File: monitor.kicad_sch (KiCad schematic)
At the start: 54 parts, among them U701 OPA2189D, U702 OPA2388D, U703 OPA2189D, U704 OPA2197xD, U705 OPA2197xD, U71 TMUX6208PWR, U72 TMUX6208PWR

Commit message: Little simplifications etc.
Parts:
- C? (x2): value 10n -> 1n
- R? (x2): value 100 -> 10
- R? (x2): value 22k -> 33k
- R?: value 13k -> 16k
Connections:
- net BufA: no longer names the net of J?.1 (Pin_1), R?.2, R?.2, RN71.5 (R4.2)
- net BufB: no longer names the net of J?.1 (Pin_1), R?.2, R?.2, RN71.7 (R2.2)
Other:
- moved on the sheet: C?, U702B, U702C

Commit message: Schematic complete, maybe
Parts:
- added C706, C707, C708, C709, C714, C715: 0u1, Capacitor_SMD:C_0402_1005Metric, symbol Device:C
- C701, C702, C703, C704: renamed from C?; footprint (none) -> Capacitor_SMD:C_0603_1608Metric; now left out of the parts list
- C705: renamed from C?; footprint (none) -> Capacitor_SMD:C_0603_1608Metric; LCSC (none) -> C307500
- C710, C711, C712, C713, C716, C717, C718, C719: renamed from C?; value 100n -> 0u1; footprint (none) -> Capacitor_SMD:C_0402_1005Metric; LCSC (none) -> C307331
- R701: renamed from R?; value 100 -> 10
- R702: renamed from R?; value 10 -> 100
- RN71: LCSC (none) -> C1358072; now left out of the parts list
- U701, U703: LCSC (none) -> C881489; now left out of the parts list
- U702: LCSC (none) -> C1517414
- U704: renamed from U705; LCSC (none) -> C139363; now left out of the parts list
- U704: LCSC (none) -> C139363; now left out of the parts list
- U71, U72: value TMUX6208PWR -> TMUX6104; footprint PW0016A-IPC_A -> Package_SO:TSSOP-14_4.4x5mm_P0.65mm; symbol Parts:TMUX6208PWR -> Parts:TMUX6104; LCSC (none) -> C2673388
- gave numbers to parts that had none: 31
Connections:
- net +18V: now also U71.12 (VDD), U72.12 (VDD), C706.1, C708.1, C714.1; no longer U71.13 (VDD), U72.13 (VDD)
- net +2V5: no longer U71.1 (A0), U72.1 (A0)
- net -18V: now also C707.2, C709.2, C715.2
- net GND: no longer U71.10 (S7), U71.12 (S5), U71.4 (S1), U71.6 (S3), U72.10 (S7), U72.12 (S5), U72.4 (S1), U72.6 (S3)
- net GNDPWR: now also U704.5 (+), U71.13 (GND), U72.13 (GND), C706.2, C707.1, C708.2, C709.1, C714.2, C715.1; no longer U704.3 (+), U71.14 (GND), U72.14 (GND)
- net IN_A1: now also U71.4 (S1); no longer U71.5 (S2)
- net IN_A2: now also U71.5 (S2); no longer U71.7 (S4)
- net IN_B1: now also U72.4 (S1); no longer U72.5 (S2)
- net IN_B2: now also U72.5 (S2); no longer U72.7 (S4)
- net SelA1: now also U71.14 (A1); no longer U71.16 (A1)
- net SelB1: now also U72.14 (A1); no longer U72.16 (A1)
- net TC+: now also U704.7; no longer U704.1
- net at C703.1, JP704.1 (A), RN71.6 (R3.2)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: now also C705.2; no longer C705.1
- net at JP702.1 (A): now also U72.6 (D); no longer U72.8 (D)
- net at R711.1, R712.2: now also U704.6 (-); no longer U704.2 (-)
- net at JP701.1 (A): now also U71.6 (D); no longer U71.8 (D)
- net at R708.1: now also C705.1; no longer C705.2
- removed net SelA2: U71.15 (A2)
- removed net SelB2: U72.15 (A2)
- new net SelA0: U71.1 (A0)
- new net SelB0: U72.1 (A0)
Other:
- moved on the sheet: C705, C710, C711, C712, C713, C716, C717, JP701, JP702, R710, R712, U701C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

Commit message: Part selection
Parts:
- J71, J72, J73, J74, J75: now left out of the parts list
- R701, R704: footprint (none) -> Resistor_SMD:R_0402_1005Metric; LCSC (none) -> C25077
- R702, R703: footprint (none) -> Resistor_SMD:R_0402_1005Metric; LCSC (none) -> C25076
- R705: footprint (none) -> Resistor_SMD:R_0603_1608Metric; LCSC (none) -> C23140
- R706, R711, R712: footprint (none) -> Resistor_SMD:R_0603_1608Metric; LCSC (none) -> C4216
- R707, R708: footprint (none) -> Resistor_SMD:R_0603_1608Metric; LCSC (none) -> C22978
- R709: footprint (none) -> Resistor_SMD:R_0603_1608Metric; LCSC (none) -> C22818
- R710: footprint (none) -> Resistor_SMD:R_0402_1005Metric; LCSC (none) -> C25741
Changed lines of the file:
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@@
 			)
 		)
-		(property "Footprint" ""
+		(property "Footprint" "Resistor_SMD:R_0402_1005Metric"
 			(at 124.46 90.932 90)
 			(effects
@@
 			)
 		)
-		(property "Datasheet" ""
+		(property "Datasheet" "~"
 			(at 124.46 92.71 0)
 			(effects
@@
 			)
 		)
+		(property "LCSC" "C25077"
+			(at 124.46 92.71 90)
+			(effects
+				(font
+					(size 1.27 1.27)
+				)
+				(hide yes)
+			)
+		)
 		(pin "2"
 		)
@@
 		(unit 1)
 		(exclude_from_sim no)
-		(in_bom yes)
+		(in_bom no)
 		(on_board yes)
 		(dnp no)
@@
 		(unit 1)
 		(exclude_from_sim no)
-		(in_bom yes)
+		(in_bom no)
 		(on_board yes)
 		(dnp no)
@@
 		(unit 1)
 		(exclude_from_sim no)
-		(in_bom yes)
+		(in_bom no)
 		(on_board yes)
 		(dnp no)
@@
 			)
 		)
-		(property "Footprint" ""
+		(property "Footprint" "Resistor_SMD:R_0603_1608Metric"
 			(at 171.45 89.408 90)
 			(effects
@@
 			)
 		)
+		(property "LCSC" "C22978"
+			(at 171.45 87.63 90)
+			(effects
+				(font
+					(size 1.27 1.27)
+				)
+				(hide yes)
+			)
+		)
 		(pin "2"
 		)
@@
 			)
 		)
-		(property "Footprint" ""
+		(property "Footprint" "Resistor_SMD:R_0603_1608Metric"
 			(at 198.12 116.078 90)
 			(effects
@@
 			)
 		)
+		(property "LCSC" "C4216"
+			(at 198.12 114.3 90)
+			(effects
+				(font
+					(size 1.27 1.27)
+				)
+				(hide yes)
+			)
+		)
 		(pin "2"
 		)
@@
 		(unit 1)
 		(exclude_from_sim no)
-		(in_bom yes)
+		(in_bom no)
 		(on_board yes)
 		(dnp no)
@@
 			)
 		)
-		(property "Footprint" ""
+		(property "Footprint" "Resistor_SMD:R_0402_1005Metric"
 			(at 124.46 81.788 90)
 			(effects
@@
 			)
 		)
-		(property "Datasheet" ""
+		(property "Datasheet" "~"
 			(at 124.46 80.01 0)
 			(effects
@@
 			)
 		)
+		(property "LCSC" "C25076"
+			(at 124.46 80.01 90)
+			(effects
+				(font
+					(size 1.27 1.27)
+				)
+				(hide yes)
+			)
+		)
 		(pin "2"
 		)
@@
 			)
 		)
-		(property "Footprint" ""
+		(property "Footprint" "Resistor_SMD:R_0603_1608Metric"
 			(at 158.75 98.552 90)
 			(effects
@@
 			)
 		)
+		(property "LCSC" "C4216"
+			(at 158.75 100.33 90)
+			(effects
+				(font
+					(size 1.27 1.27)
+				)
+				(hide yes)
+			)
+		)
 		(pin "2"
 		)
@@
 			)
 		)
-		(property "Footprint" ""
+		(property "Footprint" "Resistor_SMD:R_0402_1005Metric"
 			(at 124.46 83.312 90)
 			(effects
@@
 			)
 		)
-		(property "Datasheet" ""
+		(property "Datasheet" "~"
 			(at 124.46 85.09 0)
 			(effects
@@
 			)
 		)
+		(property "LCSC" "C25076"
+			(at 124.46 85.09 90)
+			(effects
+				(font
+					(size 1.27 1.27)
+				)
+				(hide yes)
+			)
+		)
 		(pin "2"
 		)
@@
 			)
 		)
-		(property "Footprint" ""
+		(property "Footprint" "Resistor_SMD:R_0402_1005Metric"
 			(at 124.46 74.168 90)
 			(effects
@@
 			)
 		)
-		(property "Datasheet" ""
+		(property "Datasheet" "~"
 			(at 124.46 72.39 0)
 			(effects
@@
 			)
 		)
+		(property "LCSC" "C25077"
+			(at 124.46 72.39 90)
+			(effects
+				(font
+					(size 1.27 1.27)
+				)
+				(hide yes)
+			)
+		)
 		(pin "2"
 		)
@@
 			)
 		)
-		(property "Footprint" ""
+		(property "Footprint" "Resistor_SMD:R_0402_1005Metric"
 			(at 185.42 123.698 90)
 			(effects
@@
 			)
 		)
-		(property "Datasheet" "Easy swap"
+		(property "Datasheet" "~"
 			(at 185.42 121.92 0)
 			(effects
@@
 			)
 		)
+		(property "LCSC" "C25741"
+			(at 185.42 121.92 90)
+			(effects
+				(font
+					(size 1.27 1.27)
+				)
+				(hide yes)
+			)
+		)
 		(pin "2"
 		)
@@
 			)
 		)
-		(property "Footprint" ""
+		(property "Footprint" "Resistor_SMD:R_0603_1608Metric"
 			(at 152.908 106.68 90)
 			(effects
@@
 			)
 		)
+		(property "LCSC" "C23140"
+			(at 151.13 106.68 90)
+			(effects
+				(font
+					(size 1.27 1.27)
+				)
+				(hide yes)
+			)
+		)
 		(pin "2"
 		)
@@
 			)
 		)
-		(property "Footprint" ""
+		(property "Footprint" "Resistor_SMD:R_0603_1608Metric"
 			(at 172.72 118.618 90)
 			(effects
@@
 			)
 		)
-		(property "Datasheet" "Easy swap"
+		(property "Datasheet" "~"
 			(at 172.72 116.84 0)
 			(effects
@@
 			)
 		)
+		(property "LCSC" "C22818"
+			(at 172.72 116.84 90)
+			(effects
+				(font
+					(size 1.27 1.27)
+				)
+				(hide yes)
+			)
+		)
 		(pin "2"
 		)
@@
 			)
 		)
-		(property "Footprint" ""
+		(property "Footprint" "Resistor_SMD:R_0603_1608Metric"
 			(at 215.9 123.698 90)
 			(effects
@@
 			)
 		)
+		(property "LCSC" "C4216"
+			(at 215.9 121.92 90)
+			(effects
+				(font
+					(size 1.27 1.27)
+				)
+				(hide yes)
+			)
+		)
 		(pin "2"
 		)
@@
 			)
 		)
-		(property "Footprint" ""
+		(property "Footprint" "Resistor_SMD:R_0603_1608Metric"
 			(at 181.61 93.472 90)
 			(effects
@@
 			)
 		)
+		(property "LCSC" "C22978"
+			(at 181.61 95.25 90)
+			(effects
+				(font
+					(size 1.27 1.27)
+				)
+				(hide yes)
+			)
+		)
 		(pin "2"
 		)
@@
 		(unit 1)
 		(exclude_from_sim no)
-		(in_bom yes)
+		(in_bom no)
 		(on_board yes)
 		(dnp no)

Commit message: ERC passes.
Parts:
- C703, C704: value 100p -> 0n1
- RN71: value 10k × 4 -> LT5400-1; footprint (none) -> Package_SO:MSOP-8-1EP_3x3mm_P0.65mm_EP1.68x1.88mm; symbol Device:R_Pack04 -> Parts:LT5400; R1 (none) -> 10k; R2 (none) -> 10k; R3 (none) -> 10k; R4 (none) -> 10k; now in the parts list
- U704: value OPA2197xD -> OPA2197D
- U76: renamed from U701; value OPA2189D -> OPA2189DGK; footprint Package_SO:SOIC-8_3.9x4.9mm_P1.27mm -> Package_SO:MSOP-8_3x3mm_P0.65mm; symbol Parts:OPA2189D -> Parts:OPA2189DGK
- U77: renamed from U702; value OPA2388D -> OPA2388DGK; footprint Package_SO:SOIC-8_3.9x4.9mm_P1.27mm -> Package_SO:MSOP-8_3x3mm_P0.65mm; symbol Parts:OPA2388D -> Parts:OPA2388DGK; now left out of the parts list
- U78: renamed from U703; value OPA2189D -> OPA2189DGK; footprint Package_SO:SOIC-8_3.9x4.9mm_P1.27mm -> Package_SO:MSOP-8_3x3mm_P0.65mm; symbol Parts:OPA2189D -> Parts:OPA2189DGK
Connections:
- net GNDPWR: now also RN71.9
- net TC+: now also RN71.5; no longer RN71.1 (R1.1)
- net TC-: now also RN71.4; no longer RN71.8 (R1.2)
- net at J74.1 (Pin_1), R703.2, R704.2: now also RN71.3; no longer RN71.7 (R2.2)
- net at C703.1, C705.2, JP704.1 (A)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: now also RN71.2; no longer RN71.6 (R3.2)
- net at J73.1 (Pin_1), R701.2, R702.2: now also RN71.1; no longer RN71.5 (R4.2)
- new net: C703.2, RN71.6, RN71.7, RN71.8, U77.3 (+)
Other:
- moved on the sheet: C703, R705

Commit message: Everything assigned except for wierd shit.
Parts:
- removed C716, C717: 0u1, Capacitor_SMD:C_0402_1005Metric, symbol Device:C
- removed JP701, JP702: SolderJumper_2_Bridged, symbol Jumper:SolderJumper_2_Bridged
- removed JP705, JP706, JP707, JP708, JP709, JP710, JP711, JP712, JP713, JP714, JP715, JP716: SolderJumper_2_Open, symbol Jumper:SolderJumper_2_Open
- C703: value 0n1 -> 3n3; now fitted
- C704: value 0n1 -> 330p; LCSC (none) -> C1664; now fitted; now in the parts list
- C705: value 10n -> 1n; LCSC C307500 -> (none); now left out of the parts list
- JP703: footprint (none) -> Parts:ThermJump
- R705: value 33 -> 100
- R706: value 33k -> 10k; LCSC C4216 -> (none)
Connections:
- net AddendA: now also U71.6 (D)
- net AddendB: now also U72.6 (D)
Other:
- moved on the sheet: J71, J72, J73, J75, JP703, JP704

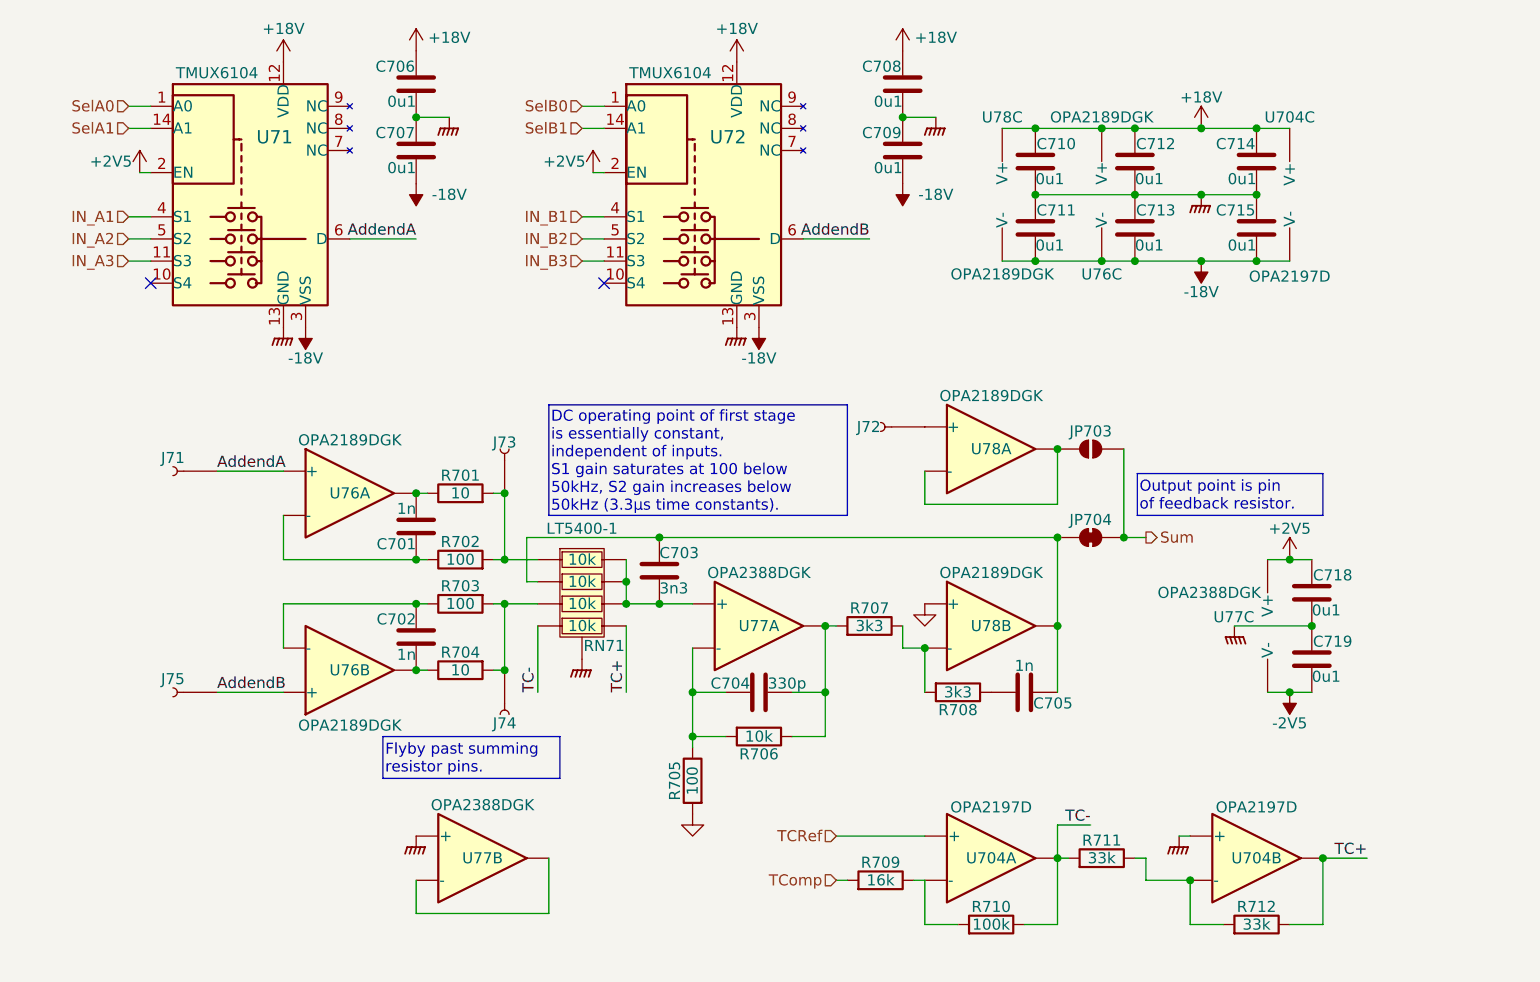
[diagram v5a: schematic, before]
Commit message: Layout underway
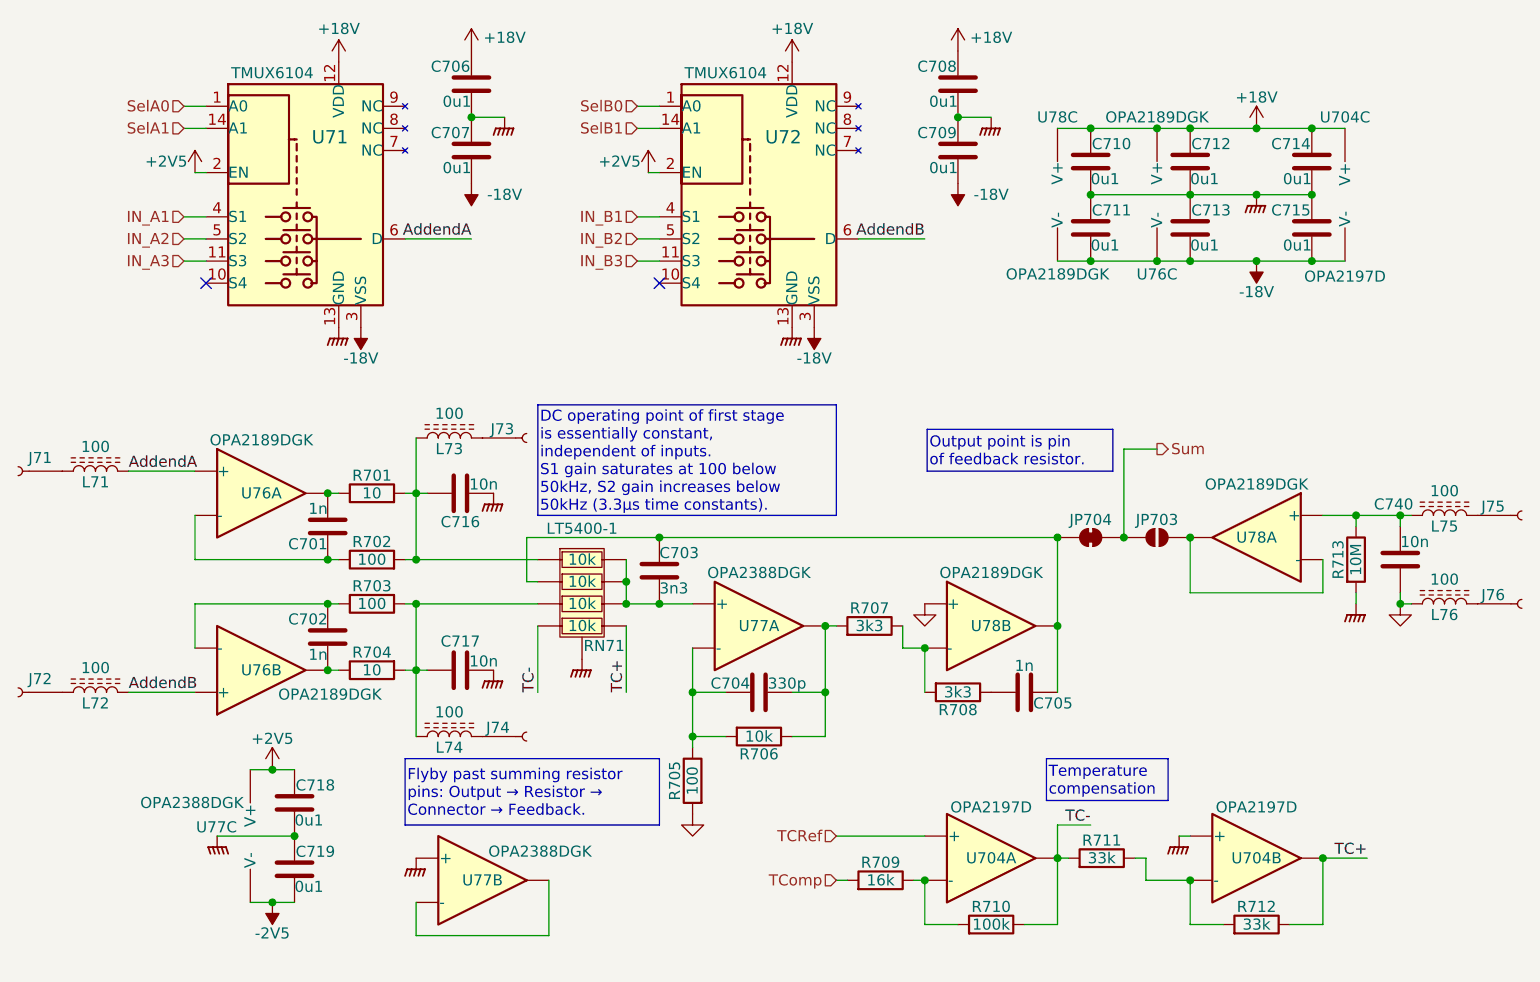
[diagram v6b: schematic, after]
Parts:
- added C716, C717, C740: 10n, Capacitor_SMD:C_0603_1608Metric, symbol Device:C
- added J76: Conn_01x01_Socket, TestPoint:TestPoint_Plated_Hole_D5.0mm, symbol Connector:Conn_01x01_Socket
- added L71, L72, L73, L74, L75, L76: 100, Inductor_SMD:L_0603_1608Metric, symbol Device:L_Ferrite
- added R713: 10M, Resistor_SMD:R_0603_1608Metric, symbol Device:R
- J71, J73, J74: footprint (none) -> TestPoint:TestPoint_Plated_Hole_D5.0mm
- J72: renamed from J75; footprint (none) -> TestPoint:TestPoint_Plated_Hole_D5.0mm
- J75: renamed from J72; footprint (none) -> TestPoint:TestPoint_Plated_Hole_D5.0mm
- JP703: footprint Parts:ThermJump -> Parts:ThermJump_1
- JP704: footprint (none) -> Parts:ThermJumpBridge
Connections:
- net AddendA: now also L71.2; no longer J71.1 (Pin_1)
- net AddendB: now also L72.2; no longer J72.1 (Pin_1)
- net GND: now also C740.2, L76.1
- net GNDPWR: now also C716.1, C717.1, R713.2
- net at U78.3 (+): now also C740.1, L75.1, R713.1; no longer J75.1 (Pin_1)
- net at R703.2, R704.2, RN71.3: now also C717.2, L74.1; no longer J74.1 (Pin_1)
- net at R701.2, R702.2, RN71.1: now also C716.2, L73.1; no longer J73.1 (Pin_1)
- new net: J74.1 (Pin_1), L74.2
- new net: J73.1 (Pin_1), L73.2
- new net: J76.1 (Pin_1), L76.2
- new net: J71.1 (Pin_1), L71.1
- new net: J72.1 (Pin_1), L72.1
- new net: J75.1 (Pin_1), L75.2
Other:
- moved on the sheet: C701, C702, C706, C707, C708, C709, C710, C711, C712, C713, C714, C715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

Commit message: Whew.  DACs routed
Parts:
- R706: LCSC (none) -> C25804
- U704: footprint Package_SO:SOIC-8_3.9x4.9mm_P1.27mm -> Parts:OPA2197; symbol Amplifier_Operational:OPA2197xD -> Parts:OPA2197D
- U76, U78: footprint Package_SO:MSOP-8_3x3mm_P0.65mm -> Parts:OPA2189
- U77: footprint Package_SO:MSOP-8_3x3mm_P0.65mm -> Parts:OPA2388
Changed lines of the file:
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@@
 			)
 		)
-		(property "Footprint" "Package_SO:MSOP-8_3x3mm_P0.65mm"
+		(property "Footprint" "Parts:OPA2189"
 			(at 217.17 77.47 0)
 			(effects
@@
 			)
 		)
-		(property "Footprint" "Package_SO:MSOP-8_3x3mm_P0.65mm"
+		(property "Footprint" "Parts:OPA2189"
 			(at 100.33 92.71 0)
 			(effects
@@
 			)
 		)
-		(property "Footprint" "Package_SO:MSOP-8_3x3mm_P0.65mm"
+		(property "Footprint" "Parts:OPA2189"
 			(at 191.77 38.1 0)
 			(effects
@@
 	)
 	(symbol
-		(lib_name "OPA2197xD_1")
-		(lib_id "Amplifier_Operational:OPA2197xD")
+		(lib_id "Parts:OPA2197D")
 		(at 215.9 114.3 0)
 		(unit 2)
@@
 			)
 		)
-		(property "Footprint" "Package_SO:SOIC-8_3.9x4.9mm_P1.27mm"
+		(property "Footprint" "Parts:OPA2197"
 			(at 218.44 114.3 0)
 			(effects
@@
 			)
 		)
-		(property "Datasheet" "1A working"
+		(property "Datasheet" "2A / 50mOhm"
 			(at 82.55 69.85 0)
 			(effects
@@
 	)
 	(symbol
-		(lib_id "Amplifier_Operational:OPA2197xD")
+		(lib_id "Parts:OPA2197D")
 		(at 226.06 38.1 0)
 		(unit 3)
@@
 			)
 		)
-		(property "Footprint" "Package_SO:SOIC-8_3.9x4.9mm_P1.27mm"
+		(property "Footprint" "Parts:OPA2197"
 			(at 228.6 38.1 0)
 			(effects
@@
 			)
 		)
-		(property "LCSC" ""
+		(property "LCSC" "C25804"
 			(at 158.75 100.33 90)
 			(effects
@@
 			)
 		)
-		(property "Datasheet" "1A working"
+		(property "Datasheet" "2A / 50mOhm"
 			(at 237.49 85.09 0)
 			(effects
@@
 			)
 		)
-		(property "Datasheet" "~"
+		(property "Datasheet" "C0G"
 			(at 147.32 81.28 0)
 			(effects
@@
 			)
 		)
-		(property "Datasheet" "1A working"
+		(property "Datasheet" "2A / 50mOhm"
 			(at 123.19 100.33 0)
 			(effects
@@
 			)
 		)
-		(property "Footprint" "Package_SO:MSOP-8_3x3mm_P0.65mm"
+		(property "Footprint" "Parts:OPA2189"
 			(at 203.2 38.1 0)
 			(effects
@@
 			)
 		)
-		(property "Datasheet" "1A working"
+		(property "Datasheet" "2A / 50mOhm"
 			(at 123.19 66.04 0)
 			(effects
@@
 	)
 	(symbol
-		(lib_name "OPA2388DGK_2")
 		(lib_id "Parts:OPA2388DGK")
 		(at 158.75 87.63 0)
@@
 			)
 		)
-		(property "Footprint" "Package_SO:MSOP-8_3x3mm_P0.65mm"
+		(property "Footprint" "Parts:OPA2388"
 			(at 161.29 87.63 0)
 			(effects
@@
 			)
 		)
-		(property "Footprint" "Package_SO:MSOP-8_3x3mm_P0.65mm"
+		(property "Footprint" "Parts:OPA2388"
 			(at 97.79 111.76 0)
 			(effects
@@
 	)
 	(symbol
-		(lib_name "OPA2197xD_2")
-		(lib_id "Amplifier_Operational:OPA2197xD")
+		(lib_id "Parts:OPA2197D")
 		(at 185.42 114.3 0)
 		(unit 1)
@@
 			)
 		)
-		(property "Footprint" "Package_SO:SOIC-8_3.9x4.9mm_P1.27mm"
+		(property "Footprint" "Parts:OPA2197"
 			(at 187.96 114.3 0)
 			(effects
@@
 			)
 		)
-		(property "Datasheet" "1A working"
+		(property "Datasheet" "2A / 50mOhm"
 			(at 237.49 74.93 0)
 			(effects
@@
 			)
 		)
-		(property "Datasheet" "1A working"
+		(property "Datasheet" "2A / 50mOhm"
 			(at 82.55 95.25 0)
 			(effects
@@
 			)
 		)
-		(property "Footprint" "Package_SO:MSOP-8_3x3mm_P0.65mm"
+		(property "Footprint" "Parts:OPA2189"
 			(at 184.15 87.63 0)
 			(effects
@@
 			)
 		)
-		(property "Footprint" "Package_SO:MSOP-8_3x3mm_P0.65mm"
+		(property "Footprint" "Parts:OPA2189"
 			(at 100.33 72.39 0)
 			(effects
@@
 	)
 	(symbol
-		(lib_name "OPA2388DGK_1")
 		(lib_id "Parts:OPA2388DGK")
 		(at 127 116.84 0)
@@
 			)
 		)
-		(property "Footprint" "Package_SO:MSOP-8_3x3mm_P0.65mm"
+		(property "Footprint" "Parts:OPA2388"
 			(at 129.54 116.84 0)
 			(effects
